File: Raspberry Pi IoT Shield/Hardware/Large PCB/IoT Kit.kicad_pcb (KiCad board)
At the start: 2 copper layers, 65 x 56 mm, 33 parts, among them J1 RPi_GPIO, SW1 SW_Push, SW2 SW_Push, U1 DHT11, U2 PCF8591

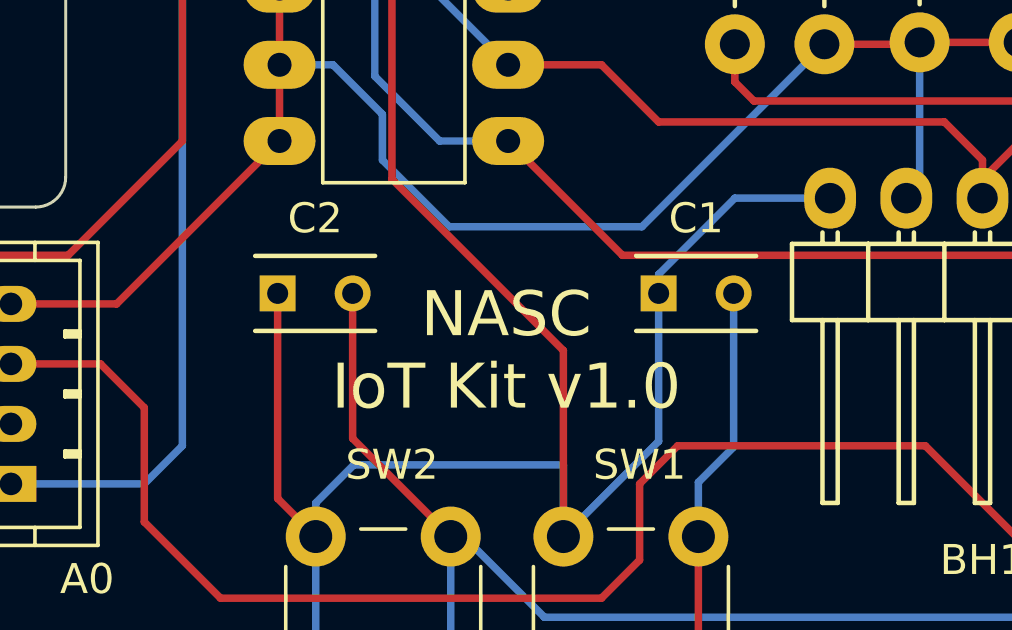
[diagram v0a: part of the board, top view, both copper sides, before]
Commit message: Reorganized directory
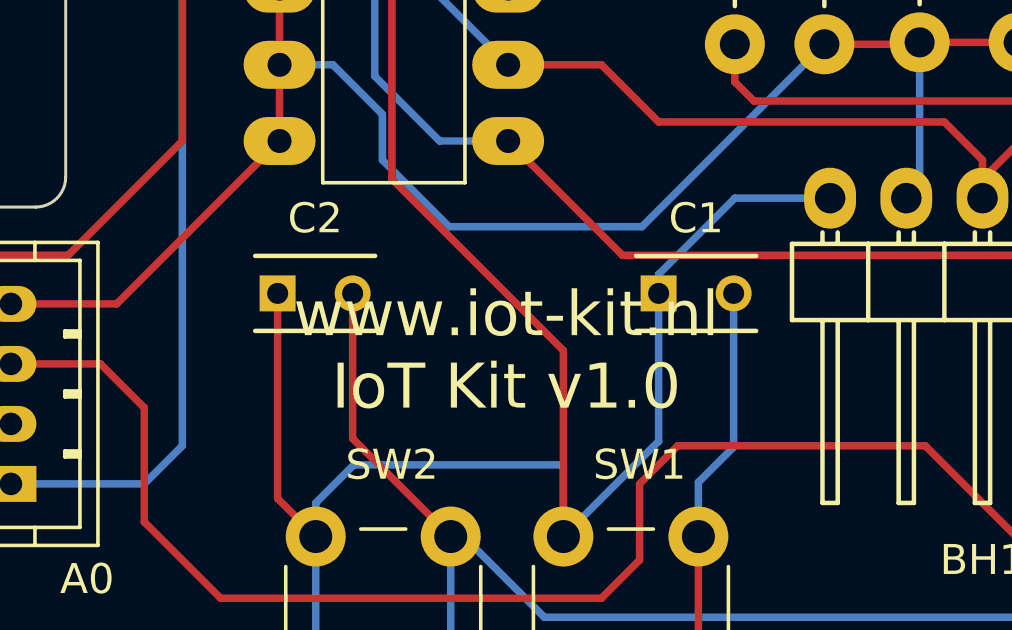
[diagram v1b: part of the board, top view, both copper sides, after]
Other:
- board text added: "www.iot-kit.nl IoT Kit v1.0"
- board text removed: "NASC IoT Kit v1.0"
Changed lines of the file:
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@@
-(kicad_pcb (version 4) (host pcbnew 4.0.6)
+(kicad_pcb (version 20171130) (host pcbnew "(5.0.0-rc2-122-g4186626)")
   (general
-    (links 65)
-    (no_connects 0)
-    (area 27.889999 27.881999 92.990001 83.982001)
     (thickness 1.6)
     (drawings 37)
@@
       (layerselection 0x01130_80000001)
       (usegerberextensions false)
+      (usegerberattributes false)
+      (usegerberadvancedattributes false)
+      (creategerberjobfile false)
       (excludeedgelayer false)
       (linewidth 0.100000)
@@
       (hpglpennumber 1)
       (hpglpenspeed 20)
-      (hpglpendiameter 15)
-      (hpglpenoverlay 2)
+      (hpglpendiameter 15.000000)
       (psnegative false)
       (psa4output false)
@@
     (descr "Through hole pin header")
     (tags "pin header")
-    (fp_text reference U1 (at 3.302 -2.794 360) (layer F.SilkS)
+    (fp_text reference U1 (at 3.302 -2.794) (layer F.SilkS)
       (effects (font (size 1 1) (thickness 0.15)))
     )
@@
       (net 14 GNDD))
     (model Pin_Headers.3dshapes/Pin_Header_Angled_1x04.wrl
-      (at (xyz 0 -0.15 0))
+      (offset (xyz 0 -3.809999942779541 0))
       (scale (xyz 1 1 1))
       (rotate (xyz 0 0 90))
@@
       (effects (font (size 1 1) (thickness 0.15)))
     )
-    (fp_text value RPi_GPIO (at 5.08 0 360) (layer F.Fab)
+    (fp_text value RPi_GPIO (at 5.08 0) (layer F.Fab)
       (effects (font (size 1 1) (thickness 0.15)))
     )
@@
     (descr "Resistor, Axial, RM 15mm,")
     (tags "Resistor Axial RM 15mm")
-    (fp_text reference R1 (at 6.858 -0.0635 450) (layer F.SilkS)
+    (fp_text reference R1 (at 6.858 -0.0635 90) (layer F.SilkS)
       (effects (font (size 1 1) (thickness 0.15)))
     )
@@
       (net 14 GNDD))
     (model Resistors_ThroughHole.3dshapes/Resistor_Horizontal_RM15mm.wrl
-      (at (xyz 0.295 0 0))
+      (offset (xyz 7.49299988746643 0 0))
       (scale (xyz 0.395 0.4 0.4))
       (rotate (xyz 0 0 0))
@@
       (net 14 GNDD))
     (model Resistors_ThroughHole.3dshapes/Resistor_Horizontal_RM15mm.wrl
-      (at (xyz 0.295 0 0))
+      (offset (xyz 7.49299988746643 0 0))
       (scale (xyz 0.395 0.4 0.4))
       (rotate (xyz 0 0 0))
@@
     (descr "Resistor, Axial, RM 15mm,")
     (tags "Resistor Axial RM 15mm")
-    (fp_text reference R3 (at 7.112 0 450) (layer F.SilkS)
+    (fp_text reference R3 (at 7.112 0 90) (layer F.SilkS)
       (effects (font (size 1 1) (thickness 0.15)))
     )
@@
     (descr "Resistor, Axial, RM 15mm,")
     (tags "Resistor Axial RM 15mm")
-    (fp_text reference R4 (at 7.112 0 450) (layer F.SilkS)
+    (fp_text reference R4 (at 7.112 0 90) (layer F.SilkS)
       (effects (font (size 1 1) (thickness 0.15)))
     )
@@
       (net 24 "Net-(C1-Pad2)"))
     (model Resistors_ThroughHole.3dshapes/Resistor_Horizontal_RM15mm.wrl
-      (at (xyz 0.295 0 0))
+      (offset (xyz 7.49299988746643 0 0))
       (scale (xyz 0.395 0.4 0.4))
       (rotate (xyz 0 0 0))
@@
       (net 3 +3V3))
     (model Buttons_Switches_THT.3dshapes/SW_PUSH_6mm_h9.5mm.wrl
-      (at (xyz 0.005 0 0))
+      (offset (xyz 0.1269999980926514 0 0))
       (scale (xyz 0.3937 0.3937 0.3937))
       (rotate (xyz 0 0 0))
@@
       (net 3 +3V3))
     (model Buttons_Switches_THT.3dshapes/SW_PUSH_6mm_h9.5mm.wrl
-      (at (xyz 0.005 0 0))
+      (offset (xyz 0.1269999980926514 0 0))
       (scale (xyz 0.3937 0.3937 0.3937))
       (rotate (xyz 0 0 0))
@@
     (descr "Resistor, Axial, RM 15mm,")
     (tags "Resistor Axial RM 15mm")
-    (fp_text reference R5 (at 7.112 0 450) (layer F.SilkS)
+    (fp_text reference R5 (at 7.112 0 90) (layer F.SilkS)
       (effects (font (size 1 1) (thickness 0.15)))
     )
@@
       (net 14 GNDD))
     (model Resistors_ThroughHole.3dshapes/Resistor_Horizontal_RM15mm.wrl
-      (at (xyz 0.295 0 0))
+      (offset (xyz 7.49299988746643 0 0))
       (scale (xyz 0.395 0.4 0.4))
       (rotate (xyz 0 0 0))
@@
     (descr "Resistor, Axial, RM 15mm,")
     (tags "Resistor Axial RM 15mm")
-    (fp_text reference R6 (at 7.112 0 450) (layer F.SilkS)
+    (fp_text reference R6 (at 7.112 0 90) (layer F.SilkS)
       (effects (font (size 1 1) (thickness 0.15)))
     )
@@
       (net 14 GNDD))
     (model Resistors_ThroughHole.3dshapes/Resistor_Horizontal_RM15mm.wrl
-      (at (xyz 0.295 0 0))
+      (offset (xyz 7.49299988746643 0 0))
       (scale (xyz 0.395 0.4 0.4))
       (rotate (xyz 0 0 0))
@@
       (net 14 GNDD))
     (model Resistors_ThroughHole.3dshapes/Resistor_Horizontal_RM15mm.wrl
-      (at (xyz 0.295 0 0))
+      (offset (xyz 7.49299988746643 0 0))
       (scale (xyz 0.395 0.4 0.4))
       (rotate (xyz 0 0 0))
@@
     (descr "Resistor, Axial, RM 15mm,")
     (tags "Resistor Axial RM 15mm")
-    (fp_text reference R8 (at 7.112 0 450) (layer F.SilkS)
+    (fp_text reference R8 (at 7.112 0 90) (layer F.SilkS)
       (effects (font (size 1 1) (thickness 0.15)))
     )
@@
       (net 14 GNDD))
     (model Resistors_ThroughHole.3dshapes/Resistor_Horizontal_RM15mm.wrl
-      (at (xyz 0.295 0 0))
+      (offset (xyz 7.49299988746643 0 0))
       (scale (xyz 0.395 0.4 0.4))
       (rotate (xyz 0 0 0))
@@
       (net 25 "Net-(C2-Pad2)"))
     (model Resistors_ThroughHole.3dshapes/Resistor_Horizontal_RM15mm.wrl
-      (at (xyz 0.295 0 0))
+      (offset (xyz 7.49299988746643 0 0))
       (scale (xyz 0.395 0.4 0.4))
       (rotate (xyz 0 0 0))
@@
       (net 14 GNDD))
     (model Resistors_ThroughHole.3dshapes/Resistor_Horizontal_RM15mm.wrl
-      (at (xyz 0.295 0 0))
+      (offset (xyz 7.49299988746643 0 0))
       (scale (xyz 0.395 0.4 0.4))
       (rotate (xyz 0 0 0))
@@
       (net 14 GNDD))
     (model Resistors_ThroughHole.3dshapes/Resistor_Horizontal_RM15mm.wrl
-      (at (xyz 0.295 0 0))
+      (offset (xyz 7.49299988746643 0 0))
       (scale (xyz 0.395 0.4 0.4))
       (rotate (xyz 0 0 0))
@@
     (descr "Through hole pin header")
     (tags "pin header")
-    (fp_text reference BH1 (at 12.065 5.08 360) (layer F.SilkS)
+    (fp_text reference BH1 (at 12.065 5.08) (layer F.SilkS)
       (effects (font (size 1 1) (thickness 0.15)))
     )
@@
       (net 3 +3V3))
     (model Pin_Headers.3dshapes/Pin_Header_Angled_1x05.wrl
-      (at (xyz 0 -0.2 0))
+      (offset (xyz 0 -5.079999923706055 0))
       (scale (xyz 1 1 1))
       (rotate (xyz 0 0 90))
@@
     (descr "JST PH series connector, B4B-PH-K, top entry type, through hole, Datasheet: http://www.jst-mfg.com/product/pdf/eng/ePH.pdf")
     (tags "connector jst ph")
-    (fp_text reference I2C-1 (at -3.81 0.635 360) (layer F.SilkS)
+    (fp_text reference I2C-1 (at -3.81 0.635) (layer F.SilkS)
       (effects (font (size 1 1) (thickness 0.15)))
     )
@@
       (net 8 GPIO16))
     (model Resistors_ThroughHole.3dshapes/Resistor_Horizontal_RM15mm.wrl
-      (at (xyz 0.295 0 0))
+      (offset (xyz 7.49299988746643 0 0))
       (scale (xyz 0.395 0.4 0.4))
       (rotate (xyz 0 0 0))
     )
   )
-  (gr_text "NASC\nIoT Kit v1.0" (at 47.625 69.215) (layer F.SilkS)
+  (gr_text "www.iot-kit.nl\nIoT Kit v1.0" (at 47.625 69.215) (layer F.SilkS)
     (effects (font (size 1.5 1.5) (thickness 0.3)))
   )
